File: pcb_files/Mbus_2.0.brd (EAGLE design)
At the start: 113 x 78.7 mm, 50 parts, among them IC1 NCP1117ST50T3G, IC4 RTC_PCF8523T, J1 F-1X18-SIP-100-32Y, J2 USB_A_SMT_FEMALE, Q1 BSS138, Q2 32.768, Q3 BSS138, Q5 BSS138, T1 2N3904, U1 ATMEGA328P-AU, Y1 CSTCE16M0V53-R0 16MHZ

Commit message: board 2.0
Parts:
- removed C1: 22p, SmartPrj:C0603-ROUND
- removed D3: CD1206-S01575, diode:MINIMELF
- removed Q5: BSS138, adafruit:SOT23
- removed R10, R11, R12, R18: 10k, SmartPrj:R0603-ROUND
- removed R19: 1M, SmartPrj:R0603-ROUND
- removed RESET: TS42031-160R-TR-7260, SmartPrj:TS42
- removed Y1: CSTCE16M0V53-R0 16MHZ, SmartPrj:RESONATOR
- added C3, C4, C5: 0.1uF, SparkFun:0805
- added C6: (no value), rcl:C0805
- added Q4: CSM-7X-DU, crystal:CSM-7X-DU
- added S2: Reset, SparkFun:TACTILE_SWITCH_SMD
- C7: value 100n -> (none); device rcl:C0805RND -> rcl:C0805
- R1: value 10k -> 10K; device SmartPrj:R0603-ROUND -> SparkFun:0805
- moved C7 135.5 mm to (-9.00, -57.5)
- moved R1 117.9 mm to (-6.55, -42.8)
- moved R16 96.9 mm to (-9.50, -47.4), turned to 0 degrees
- moved T1 92.8 mm to (-8.27, -52.7)
- moved R17 89.5 mm to (-5.13, -47.4)
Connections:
- removed net 5-GND: RESET.5
- removed net CGND: C7.2, U1.21
- removed net N$12: PIHEADER.19, Q3.2, R15.1
- removed net N$15: PIHEADER.23, Q5.2, R18.1
- removed net N$5: PIHEADER.21, Q1.2, R3.1
- removed net VCC: U1.6
- removed net VCC_2: U1.4
- new net N$14: C4.2, U1.20
- new net PISCL: PIHEADER.35, Q3.2, R15.1
- new net PISDA: PIHEADER.12, Q1.2, R3.1
- new net RESET1: C5.1, R1.1, S2.3, S2.4, U1.29
- net +3V3: no longer Q5.1, R18.2
- net +5V: now also C3.2, U1.4, U1.6; no longer C7.1, D3.C, R10.1, R11.1, R12.1
- net GND: now also C3.1, C4.1, C6.1, C7.1, S2.1, S2.2, U1.21, U1.3, U1.5; no longer C1.2, RESET.1, RESET.2, Y1.2
- net MISO: no longer Q1.3, R2.1
- net MOSI: no longer Q3.3, R14.1
- net N$1: now also C6.2, Q4.1; no longer R19.1, Y1.3
- net N$13: now also C7.2, Q4.2; no longer R19.2, Y1.1
- net RESET: now also C5.2; no longer C1.1, D3.A, R10.2, RESET.3, RESET.4, U1.29
- net SCL: now also Q3.3, R14.1; no longer R11.2
- net SCLK: no longer Q5.3, R1.1
- net SDA: now also Q1.3, R2.1; no longer R12.2
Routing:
- net N$15: track 131.1 -> 0.00 mm, vias 3 -> 0
- net +3V3: track 123.2 -> 0.00 mm, vias 5 -> 0
- net RESET: track 113.6 -> 0.00 mm, vias 2 -> 0
- net N$5: track 109.7 -> 0.00 mm, vias 1 -> 0
- net SDA: track 103.7 -> 0.00 mm, vias 2 -> 0
- net SCL: track 99.5 -> 0.00 mm, vias 2 -> 0
- net N$12: track 94.1 -> 0.00 mm, vias 2 -> 0
- net PD4: track 91.9 -> 0.00 mm, vias 1 -> 0
- net PD5: track 89.6 -> 0.00 mm, vias 1 -> 0
- net GND: track 79.7 -> 0.00 mm, vias 4 -> 0
- net RX: track 73.9 -> 0.00 mm
- net PD3: track 64.6 -> 0.00 mm, vias 3 -> 0
- net PD2: track 64.3 -> 0.00 mm, vias 1 -> 0
- net MOSI: track 62.7 -> 0.00 mm, vias 1 -> 0
- net MISO: track 60.7 -> 0.00 mm, vias 3 -> 0
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
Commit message: pcb layout of 2.0
Signed-off-by: Yiteng Cai <alonsochate@umich.edu>
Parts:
- POWER: value 8x1F-H8.5 -> (none); device SmartPrj:1X08 -> pinhead:1X03
- moved C7 133.3 mm to (34.3, 68.6)
- moved R16 110.6 mm to (52.1, 44.5), turned to 270 degrees
- moved T1 104.3 mm to (46.6, 36.1), flipped to the bottom
- moved C6 103.0 mm to (34.3, 58.4)
- moved C4 101.1 mm to (65.3, 51.2), turned to 90 degrees
- moved C5 98.3 mm to (61.4, 25.4), turned to 180 degrees
- moved Q4 97.4 mm to (41.9, 63.5), turned to 90 degrees
- moved C3 96.1 mm to (61.5, 51.3), turned to 90 degrees
- moved R17 92.5 mm to (45.0, 30.4), turned to 270 degrees
- moved R1 90.9 mm to (58.8, 20.4), turned to 270 degrees
- moved S2 77.6 mm to (47.0, 16.5), turned to 90 degrees
- moved Q2 69.3 mm to (96.7, 50.1), flipped to the top
- moved J3 60.9 mm to (20.3, 2.54)
- moved B2 60.9 mm to (88.0, 22.5), flipped to the top, turned to 180 degrees
- moved D1 58.2 mm to (24.1, 11.4), turned to 180 degrees
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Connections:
- new net VCC: U1.6
- net +5V: now also POWER.1; no longer POWER.4, POWER.5, U1.6
- net GND: now also POWER.3; no longer POWER.6, POWER.7, POWER.8
- net RESET: no longer POWER.3
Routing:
- net SDA: track 0.00 -> 109.0 mm, vias 0 -> 5
- net SCL: track 0.00 -> 106.6 mm, vias 0 -> 6
- net GND: track 0.00 -> 100.1 mm, vias 0 -> 5
- net RX: track 0.00 -> 85.8 mm, vias 0 -> 2
- net TX: track 0.00 -> 85.2 mm, vias 0 -> 2
- net PD4: track 0.00 -> 73.4 mm
- net PD5: track 0.00 -> 71.9 mm, vias 0 -> 1
- net RESET1: track 0.00 -> 70.8 mm
- net +3V3: track 0.00 -> 58.2 mm
- net PD2: track 0.00 -> 58.1 mm, vias 0 -> 2
- net PD7: track 0.00 -> 57.5 mm
- net PD3: track 0.00 -> 55.1 mm
- net OUT: track 0.00 -> 53.8 mm, vias 0 -> 1
- net +5V: track 0.00 -> 47.7 mm, vias 0 -> 9
- net PISCL: track 0.00 -> 43.3 mm
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- added copper zone on layer 1, net GND
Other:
- board text removed: "MBUS BOARD v1.2"

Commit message: pcb 2.0
Signed-off-by: Yiteng Cai <alonsochate@umich.edu>
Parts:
- moved R17 20.2 mm to (33.0, 46.6), turned to 180 degrees
- moved PIHEADER 7.39 mm to (7.79, 30.7)
- moved Q3 1.47 mm to (32.5, 43.1)
- moved R15 1.41 mm to (24.1, 43.0)
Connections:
- removed net PC5: J1.5
- net +3V3: now also R17.2
- net +5V: no longer R17.2
- net PC1: now also J1.5
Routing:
- net PC1: track 0.00 -> 53.2 mm, vias 0 -> 1
- net PISCL: track 43.3 -> 61.2 mm
- net OUT: track 53.8 -> 62.6 mm, vias 1 -> 2
- net +3V3: track 58.2 -> 54.6 mm
- net PISDA: track 24.9 -> 27.8 mm
- net SCL: track 106.6 -> 107.6 mm
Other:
- board text added: "MBUS BOARD v2.0"

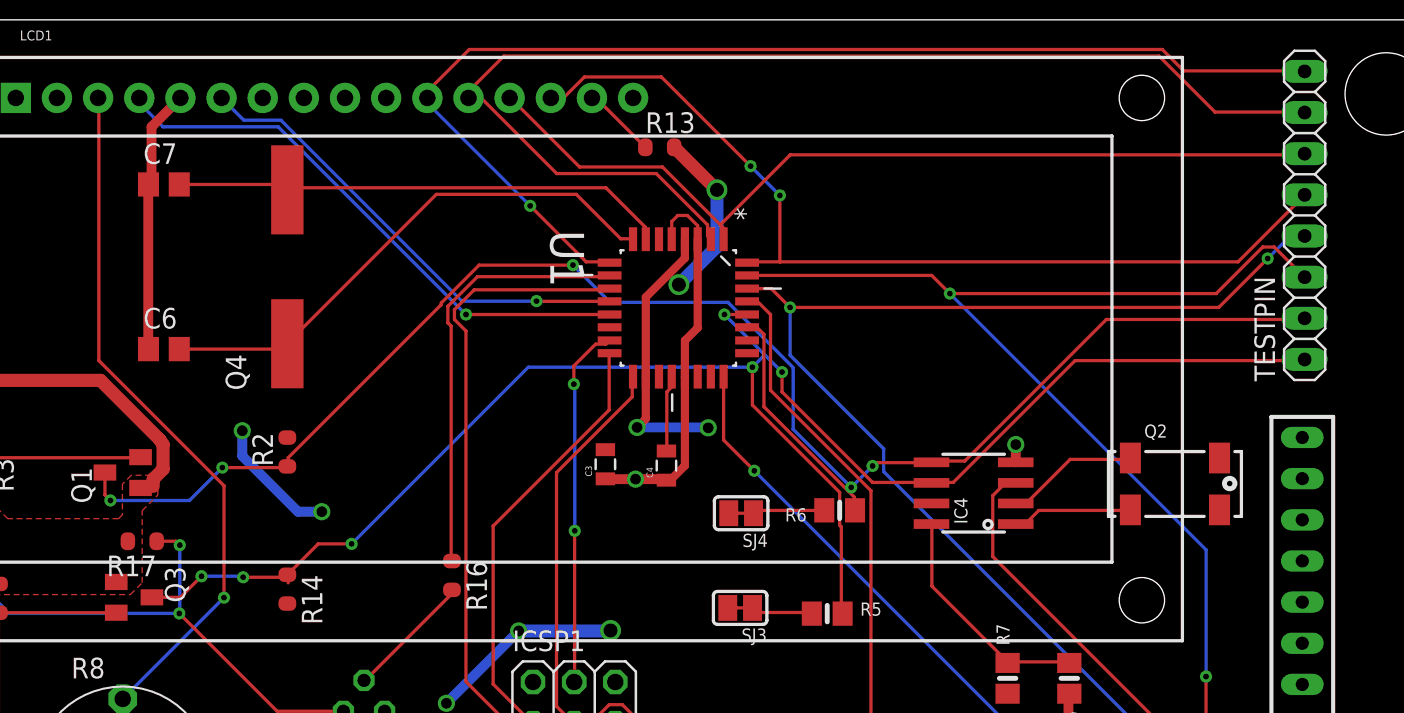
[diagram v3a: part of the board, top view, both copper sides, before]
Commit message: Modify the traces and generate gerber file
Signed-off-by: Yiteng Cai <alonsochate@umich.edu>
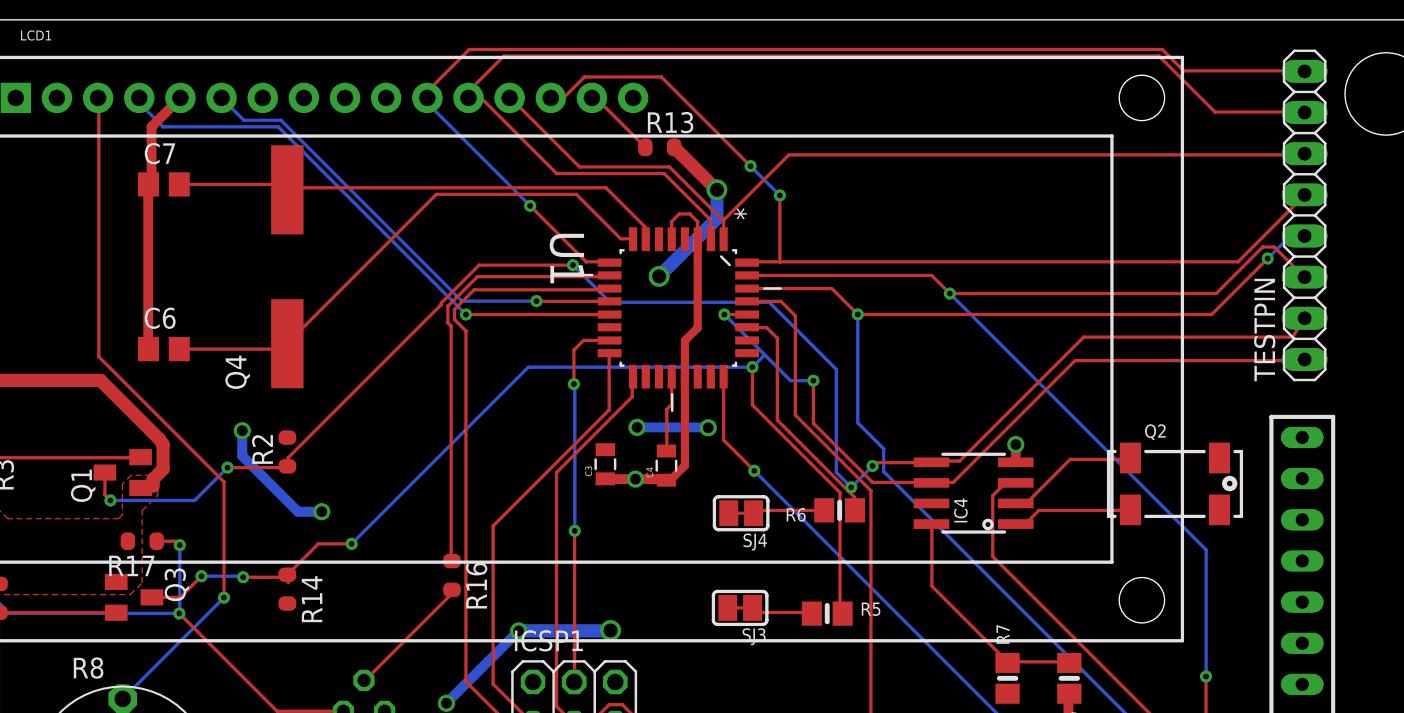
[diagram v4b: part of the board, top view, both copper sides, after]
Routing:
- net +5V: track 47.7 -> 34.8 mm
- net SDA: track 109.0 -> 111.0 mm
- net RX: track 85.8 -> 84.0 mm
- net RESET1: track 70.8 -> 71.6 mm
- net SCL: track 107.6 -> 108.5 mm
- net MOSI: track 22.5 -> 23.1 mm
